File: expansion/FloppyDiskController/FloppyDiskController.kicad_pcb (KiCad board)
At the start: 2 copper layers, 111.8 x 70.6 mm, 22 parts, among them J1 D68K_64PIN_BOARD, J2 JTAG, J3 FloppyHeader, J4 Conn_01x04, Q1 2N4403, U1 74LS125, U2 XC9536PC44, U3 WD37C65C, X1 16MHz

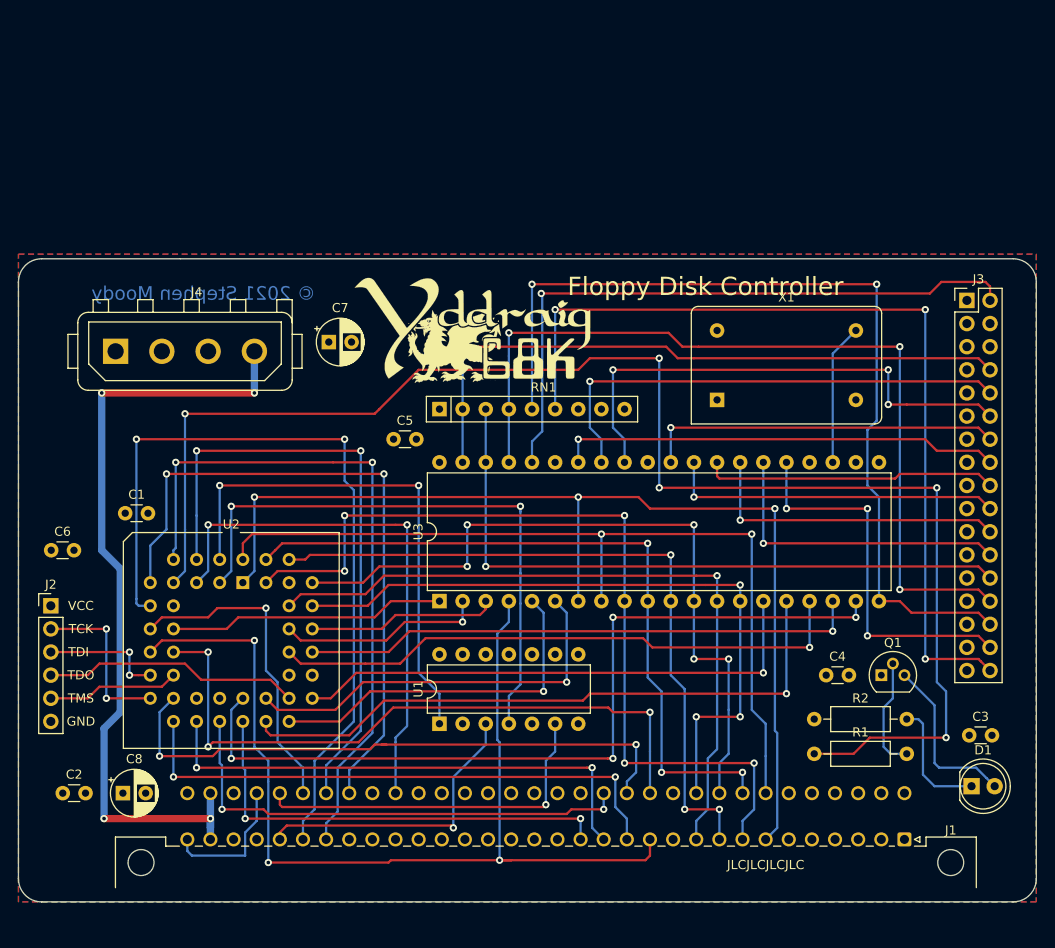
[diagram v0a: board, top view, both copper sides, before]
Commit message: Changed PCB layout to 100x100 baord
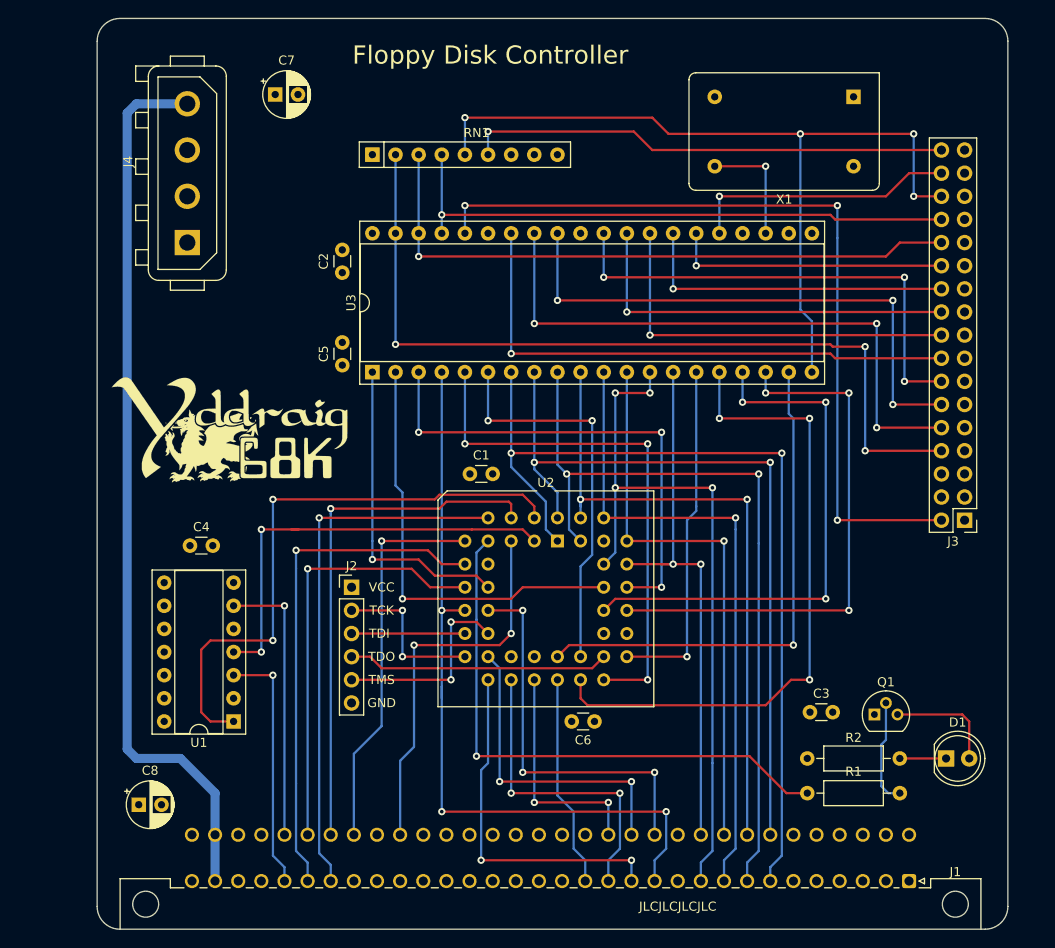
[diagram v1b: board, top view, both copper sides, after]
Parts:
- U1: footprint Package_DIP:DIP-14_W7.62mm -> Package_DIP:DIP-14_W7.62mm_Socket
- U3: footprint Package_DIP:DIP-40_W15.24mm -> Package_DIP:DIP-40_W15.24mm_Socket
- moved C4 71.3 mm to (105.2, 87.9)
- moved C2 64.9 mm to (121.9, 57.9), turned to 90 degrees
- moved C6 62.5 mm to (149.6, 107.2), turned to 180 degrees
- moved C1 38.1 mm to (135.9, 80.0)
- moved X1 36.5 mm to (178.1, 38.6), turned to 180 degrees
- moved U2 34.8 mm to (145.5, 87.4)
- moved J2 33.1 mm to (122.9, 92.5)
- moved RN1 28.9 mm to (125.2, 45.0)
- moved G*** 28.8 mm to (109.7, 74.9)
- moved C7 27.8 mm to (114.6, 38.4)
- moved U3 26.2 mm to (125.2, 68.8)
- moved J3 24.1 mm to (190.2, 85.1), turned to 180 degrees
- moved U1 22.6 mm to (110.0, 107.2), turned to 180 degrees
- moved C3 17.7 mm to (173.3, 106.2)
- moved J4 14.3 mm to (104.9, 54.6), turned to 90 degrees
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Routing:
- net LED: track 161.4 -> 62.2 mm, vias 5 -> 1
- net Net-(J3-Pad34): track 97.6 -> 53.2 mm, vias 3 -> 1
- net FDC_RST: track 93.0 -> 56.6 mm, vias 4 -> 1
- net FDC_CS: track 20.8 -> 54.1 mm, vias 0 -> 3
- net CS_REG: track 89.2 -> 56.0 mm, vias 2 -> 1
- net /A4: track 66.1 -> 34.6 mm
- net Net-(J3-Pad28): track 94.9 -> 63.7 mm, vias 3 -> 1
- net /A2: track 73.6 -> 42.9 mm
- net UDS: track 73.2 -> 42.7 mm, vias 2 -> 1
- net /A6: track 53.9 -> 25.1 mm
- net /A7: track 49.9 -> 23.4 mm, vias 2 -> 0
- net /A1: track 111.3 -> 84.9 mm
- net WR: track 22.7 -> 47.8 mm
- net /A3: track 62.0 -> 38.9 mm
- net /A5: track 56.9 -> 34.6 mm
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- added copper zone on In2.Cu, net +5V
- added copper zone on In1.Cu, net GND
- removed copper zone on F.Cu, net +5V
- removed copper zone on B.Cu, net GND
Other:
- board size 111.8 x 70.6 mm -> 100 x 100 mm
- copper layers 2 -> 4
- net class POWER added: clearance 0.2, trace_width 0.5, via_dia 0.8, via_drill 0.4
- net class SIGNAL added: clearance 0.2, trace_width 0.25, via_dia 0.8, via_drill 0.4
- board text removed: "© 2021 Stephen Moody"

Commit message: Generated gerber files
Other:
- board text added: "FDC-WD37C65C"
- board text added: "© 2021 Stephen Moody"
- board text removed: "Floppy Disk Controller"

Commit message: More progress on VGA card design
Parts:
- R1: value 10K -> 1K
- R2: value R -> 150R

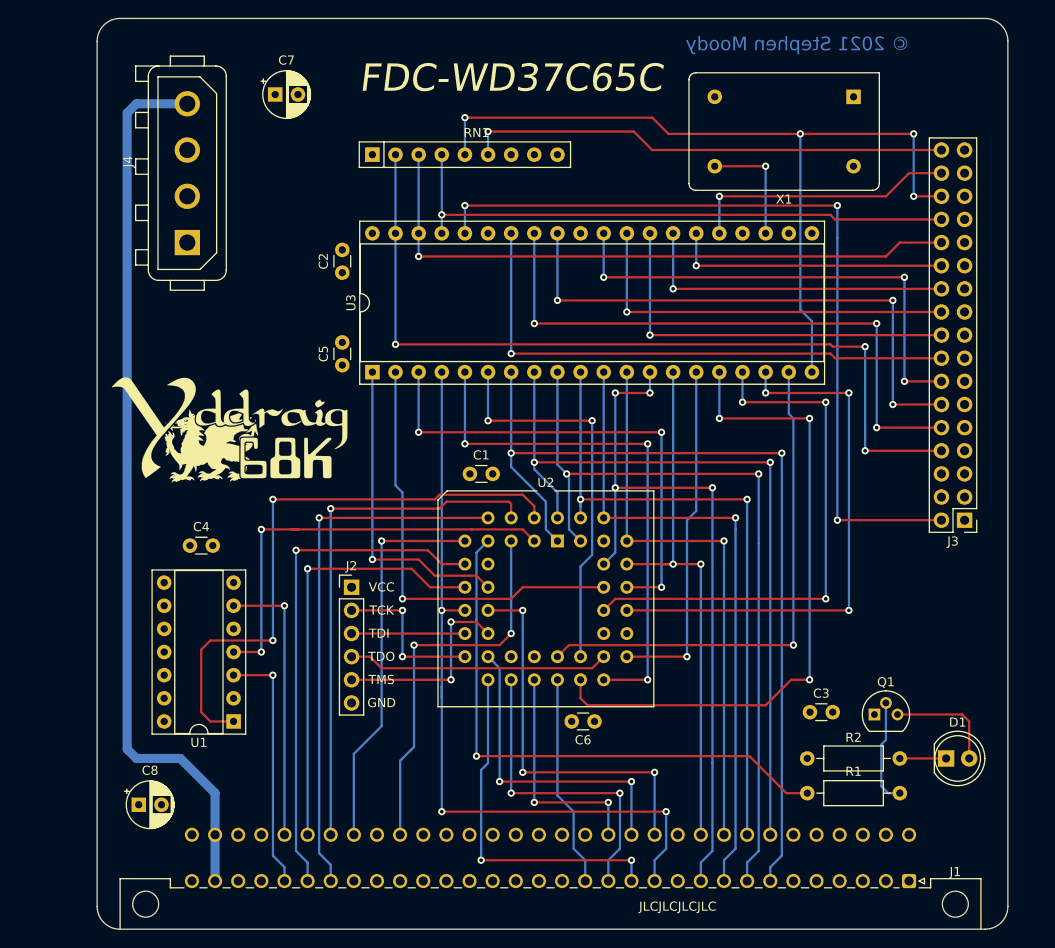
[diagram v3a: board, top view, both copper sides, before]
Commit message: Updated to KiCAD6
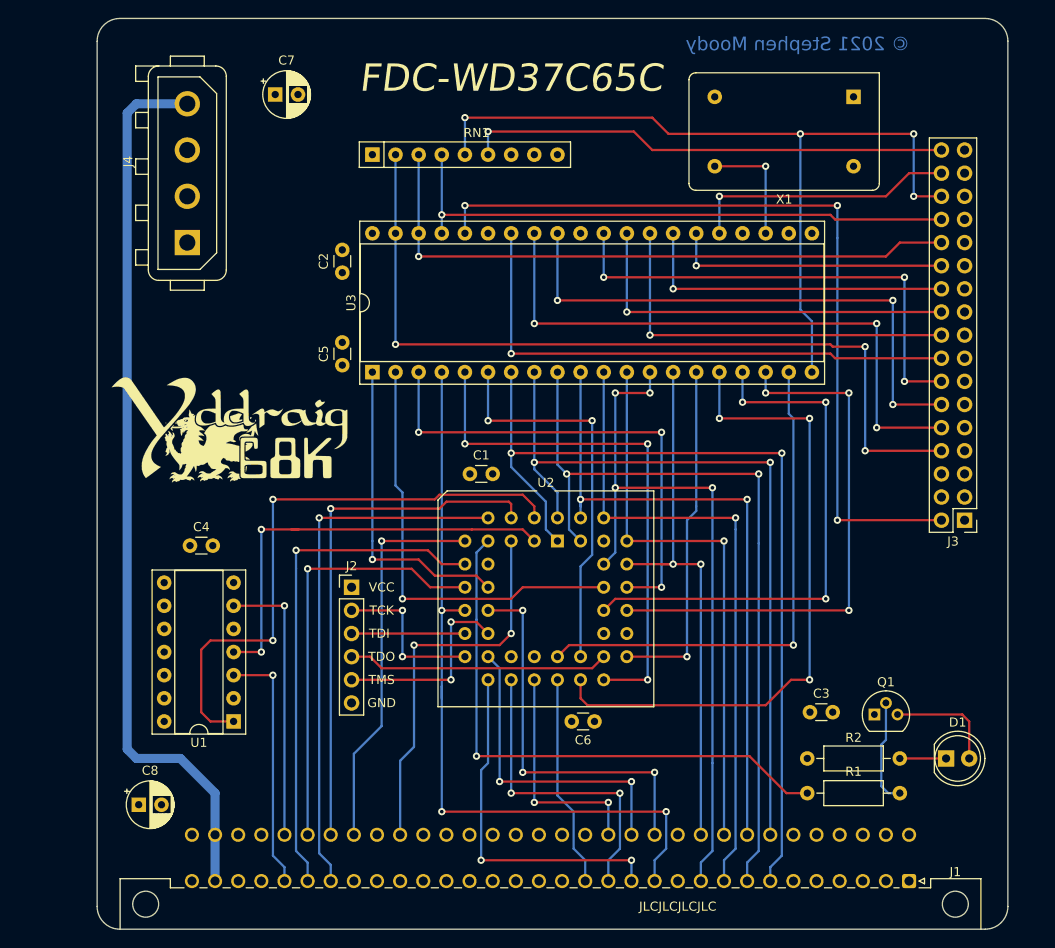
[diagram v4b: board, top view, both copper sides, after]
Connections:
- J1 pad A16: Net-(J1-PadA16) -> unconnected-(J1-PadA16)
- J1 pad A17: Net-(J1-PadA17) -> unconnected-(J1-PadA17)
- J1 pad A18: Net-(J1-PadA18) -> unconnected-(J1-PadA18)
- J1 pad A19: Net-(J1-PadA19) -> unconnected-(J1-PadA19)
- J1 pad A20: Net-(J1-PadA20) -> unconnected-(J1-PadA20)
- J1 pad A21: Net-(J1-PadA21) -> unconnected-(J1-PadA21)
- J1 pad A22: Net-(J1-PadA22) -> unconnected-(J1-PadA22)
- J1 pad A23: Net-(J1-PadA23) -> unconnected-(J1-PadA23)
- J1 pad A25: Net-(J1-PadA25) -> unconnected-(J1-PadA25)
- J1 pad A29: Net-(J1-PadA29) -> unconnected-(J1-PadA29)
- J1 pad A3: Net-(J1-PadA3) -> unconnected-(J1-PadA3)
- J1 pad A30: Net-(J1-PadA30) -> unconnected-(J1-PadA30)
- J1 pad A4: Net-(J1-PadA4) -> unconnected-(J1-PadA4)
- J1 pad A5: Net-(J1-PadA5) -> unconnected-(J1-PadA5)
- J1 pad A6: Net-(J1-PadA6) -> unconnected-(J1-PadA6)
- J1 pad C15: Net-(J1-PadC15) -> unconnected-(J1-PadC15)
- J1 pad C16: Net-(J1-PadC16) -> unconnected-(J1-PadC16)
- J1 pad C17: Net-(J1-PadC17) -> unconnected-(J1-PadC17)
- J1 pad C18: Net-(J1-PadC18) -> unconnected-(J1-PadC18)
- J1 pad C19: Net-(J1-PadC19) -> unconnected-(J1-PadC19)
- J1 pad C2: Net-(J1-PadC2) -> unconnected-(J1-PadC2)
- J1 pad C20: Net-(J1-PadC20) -> unconnected-(J1-PadC20)
- J1 pad C21: Net-(J1-PadC21) -> unconnected-(J1-PadC21)
- J1 pad C22: Net-(J1-PadC22) -> unconnected-(J1-PadC22)
- J1 pad C3: Net-(J1-PadC3) -> unconnected-(J1-PadC3)
- J1 pad C30: Net-(J1-PadC30) -> unconnected-(J1-PadC30)
- J1 pad C4: Net-(J1-PadC4) -> unconnected-(J1-PadC4)
- J1 pad C5: Net-(J1-PadC5) -> unconnected-(J1-PadC5)
- J1 pad C6: Net-(J1-PadC6) -> unconnected-(J1-PadC6)
- J3 pad 4: Net-(J3-Pad4) -> unconnected-(J3-Pad4)
- J3 pad 6: Net-(J3-Pad6) -> unconnected-(J3-Pad6)
- RN1 pad 7: Net-(RN1-Pad7) -> unconnected-(RN1-Pad7)
- RN1 pad 8: Net-(RN1-Pad8) -> unconnected-(RN1-Pad8)
- RN1 pad 9: Net-(RN1-Pad9) -> unconnected-(RN1-Pad9)
- U1 pad 11: Net-(U1-Pad11) -> unconnected-(U1-Pad11)
- U1 pad 8: Net-(U1-Pad8) -> unconnected-(U1-Pad8)
- U3 pad 35: Net-(U3-Pad35) -> unconnected-(U3-Pad35)
- X1 pad 1: Net-(X1-Pad1) -> unconnected-(X1-Pad1)
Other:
- net class Default removed
- net class POWER removed
- net class SIGNAL removed
